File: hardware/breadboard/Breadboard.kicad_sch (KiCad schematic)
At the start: 12 parts, among them J1 AudioPlug3, J2 Conn_01x04_Male, J3 Conn_01x04_Female, J4 USB_A, SW1 SW_Push, U1 ESP32-S3-DevKitC-1, U2 LM3525M-H, U3 D52QD2M6IA

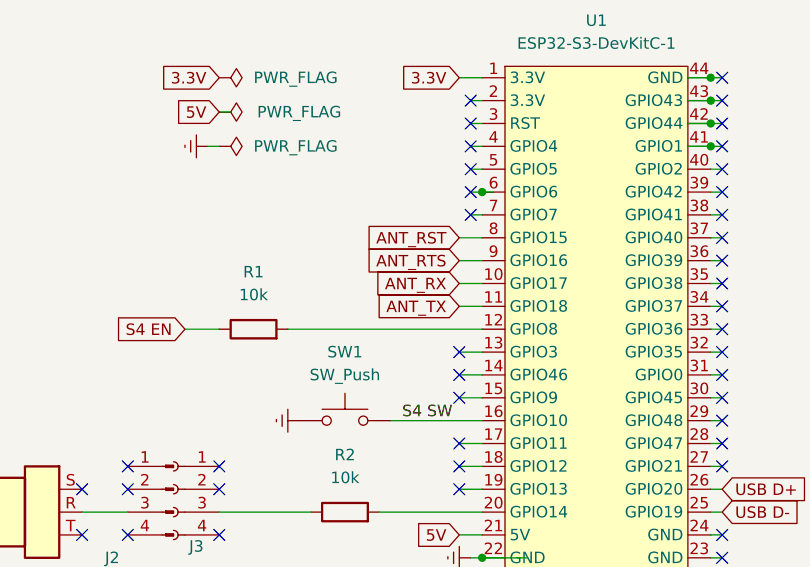
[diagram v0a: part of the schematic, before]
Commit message: sync pcb GPIO reboot on crash more error handling
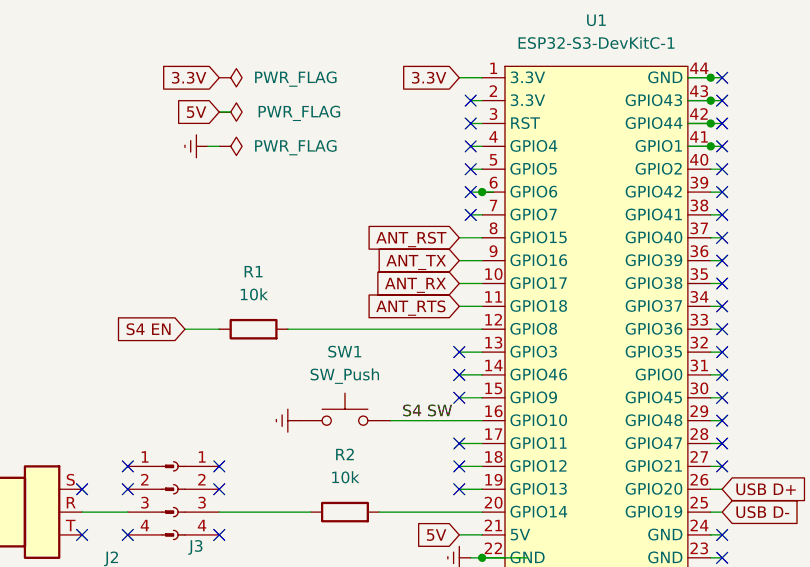
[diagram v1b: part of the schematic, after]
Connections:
- net ANT_RTS: now also U1.11 (GPIO18); no longer U1.9 (GPIO16)
- net ANT_TX: now also U1.9 (GPIO16); no longer U1.11 (GPIO18)
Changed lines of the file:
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@@
+    (stroke (width 0) (type default) (color 0 0 0 0))
+  )
+  (wire (pts (xy 135.89 85.09) (xy 138.43 85.09))
+    (stroke (width 0) (type default) (color 0 0 0 0))
+  )
+  (wire (pts (xy 186.69 107.95) (xy 190.5 107.95))
+    (stroke (width 0) (type default) (color 0 0 0 0))
+  )
+  (wire (pts (xy 189.23 102.87) (xy 190.5 102.87))
+    (stroke (width 0) (type default) (color 0 0 0 0))
+  )
+  (wire (pts (xy 163.83 77.47) (xy 165.1 77.47))
+    (stroke (width 0) (type default) (color 0 0 0 0))
+  )
+  (wire (pts (xy 163.83 64.77) (xy 165.1 64.77))
+    (stroke (width 0) (type default) (color 0 0 0 0))
+  )
+  (wire (pts (xy 163.83 118.11) (xy 165.1 118.11))
+    (stroke (width 0) (type default) (color 0 0 0 0))
+  )
+  (wire (pts (xy 137.16 74.93) (xy 138.43 74.93))
+    (stroke (width 0) (type default) (color 0 0 0 0))
+  )
+  (wire (pts (xy 163.83 87.63) (xy 165.1 87.63))
+    (stroke (width 0) (type default) (color 0 0 0 0))
+  )
+  (wire (pts (xy 163.83 67.31) (xy 165.1 67.31))
+    (stroke (width 0) (type default) (color 0 0 0 0))
+  )
+  (wire (pts (xy 128.27 102.87) (xy 138.43 102.87))
+    (stroke (width 0) (type default) (color 0 0 0 0))
+  )
+  (wire (pts (xy 93.98 113.03) (xy 99.06 113.03))
     (stroke (width 0) (type default) (color 0 0 0 0))
   )
@@
     (stroke (width 0) (type default) (color 0 0 0 0))
   )
-  (wire (pts (xy 186.69 107.95) (xy 190.5 107.95))
-    (stroke (width 0) (type default) (color 0 0 0 0))
-  )
-  (wire (pts (xy 189.23 102.87) (xy 190.5 102.87))
-    (stroke (width 0) (type default) (color 0 0 0 0))
-  )
-  (wire (pts (xy 163.83 77.47) (xy 165.1 77.47))
-    (stroke (width 0) (type default) (color 0 0 0 0))
-  )
-  (wire (pts (xy 163.83 64.77) (xy 165.1 64.77))
-    (stroke (width 0) (type default) (color 0 0 0 0))
-  )
-  (wire (pts (xy 163.83 118.11) (xy 165.1 118.11))
-    (stroke (width 0) (type default) (color 0 0 0 0))
-  )
-  (wire (pts (xy 137.16 74.93) (xy 138.43 74.93))
-    (stroke (width 0) (type default) (color 0 0 0 0))
-  )
-  (wire (pts (xy 163.83 87.63) (xy 165.1 87.63))
-    (stroke (width 0) (type default) (color 0 0 0 0))
-  )
-  (wire (pts (xy 163.83 67.31) (xy 165.1 67.31))
-    (stroke (width 0) (type default) (color 0 0 0 0))
-  )
-  (wire (pts (xy 128.27 102.87) (xy 138.43 102.87))
-    (stroke (width 0) (type default) (color 0 0 0 0))
-  )
-  (wire (pts (xy 93.98 113.03) (xy 99.06 113.03))
-    (stroke (width 0) (type default) (color 0 0 0 0))
-  )
   (wire (pts (xy 205.74 128.27) (xy 209.55 128.27))
     (stroke (width 0) (type default) (color 0 0 0 0))
@@
   )
   (wire (pts (xy 163.83 100.33) (xy 165.1 100.33))
-    (stroke (width 0) (type default) (color 0 0 0 0))
-  )
-  (wire (pts (xy 135.89 85.09) (xy 138.43 85.09))
     (stroke (width 0) (type default) (color 0 0 0 0))
   )
@@
     )
   )
-  (global_label "ANT_RTS" (shape input) (at 135.89 85.09 180) (fields_autoplaced)
-    (effects (font (size 1.27 1.27)) (justify right))
-    (property "Intersheet References" "${INTERSHEET_REFS}" (id 0) (at 125.6755 85.0106 0)
+  (global_label "ANT_RTS" (shape input) (at 135.89 90.17 180) (fields_autoplaced)
+    (effects (font (size 1.27 1.27)) (justify right))
+    (property "Intersheet References" "${INTERSHEET_REFS}" (id 0) (at 125.6755 90.0906 0)
       (effects (font (size 1.27 1.27)) (justify right) hide)
     )
@@
     )
   )
-  (global_label "ANT_TX" (shape input) (at 135.89 90.17 180) (fields_autoplaced)
-    (effects (font (size 1.27 1.27)) (justify right))
-    (property "Intersheet References" "${INTERSHEET_REFS}" (id 0) (at 126.9455 90.0906 0)
-      (effects (font (size 1.27 1.27)) (justify right) hide)
-    )
+  (global_label "ANT_TX" (shape input) (at 135.89 85.09 180) (fields_autoplaced)
+    (effects (font (size 1.27 1.27)) (justify right))
+    (property "Intersheet References" "${INTERSHEET_REFS}" (id 0) (at 126.9455 85.0106 0)
+      (effects (font (size 1.27 1.27)) (justify right) hide)
+    )
